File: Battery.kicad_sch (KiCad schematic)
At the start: 4 parts

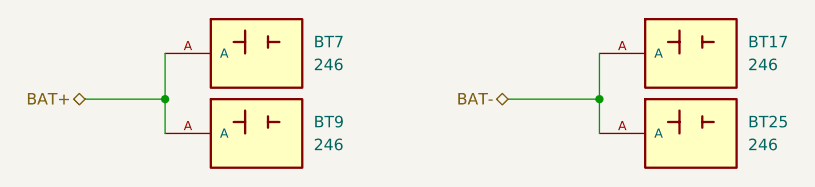
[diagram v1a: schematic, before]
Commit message: adds connectors and bom
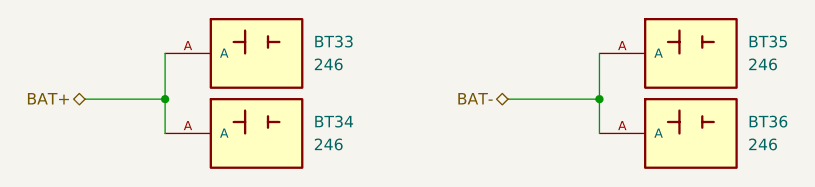
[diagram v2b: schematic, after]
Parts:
- renumbered BT7 to BT33, BT9 to BT34, BT17 to BT35, BT25 to BT36
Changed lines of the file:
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@@
 		(dnp no)
 		(fields_autoplaced yes)
-		(property "Reference" "BT17"
+		(property "Reference" "BT35"
 			(at 125.73 80.0099 0)
 			(effects
@@
 		(instances
 			(project "BounceBack"
-				(path "/f4d3aea2-c6b7-478e-bd31-9b0098518f48/1a31741d-88c3-47d9-834f-01dfee5cc6d9/1551cce4-8866-4495-982a-a77f6e9327d9"
-					(reference "BT17")
-					(unit 1)
-				)
-				(path "/f4d3aea2-c6b7-478e-bd31-9b0098518f48/1a31741d-88c3-47d9-834f-01dfee5cc6d9/117ef703-b8fc-4370-bfcd-aff31c8bd2d5"
-					(reference "BT18")
-					(unit 1)
-				)
-				(path "/f4d3aea2-c6b7-478e-bd31-9b0098518f48/1a31741d-88c3-47d9-834f-01dfee5cc6d9/b6448387-a56d-4315-8544-a7512868ec52"
-					(reference "BT19")
-					(unit 1)
-				)
-				(path "/f4d3aea2-c6b7-478e-bd31-9b0098518f48/1a31741d-88c3-47d9-834f-01dfee5cc6d9/84fcc5dc-fa9b-4edf-8bba-1647bc64b9b8"
-					(reference "BT20")
-					(unit 1)
-				)
-				(path "/f4d3aea2-c6b7-478e-bd31-9b0098518f48/1a31741d-88c3-47d9-834f-01dfee5cc6d9/918d9447-f370-4db2-b8a3-eec52e987d54"
-					(reference "BT21")
-					(unit 1)
-				)
-				(path "/f4d3aea2-c6b7-478e-bd31-9b0098518f48/1a31741d-88c3-47d9-834f-01dfee5cc6d9/c0fa25f9-89d7-46c1-befa-1ac9188fe79f"
-					(reference "BT22")
-					(unit 1)
-				)
-				(path "/f4d3aea2-c6b7-478e-bd31-9b0098518f48/1a31741d-88c3-47d9-834f-01dfee5cc6d9/1a201732-b9ac-4a68-82dc-a3b4e58f320a"
-					(reference "BT23")
-					(unit 1)
-				)
-				(path "/f4d3aea2-c6b7-478e-bd31-9b0098518f48/1a31741d-88c3-47d9-834f-01dfee5cc6d9/9db08163-0bb8-4c3b-bb41-74c13cb1f83a"
-					(reference "BT24")
+				(path "/f4d3aea2-c6b7-478e-bd31-9b0098518f48/afea23a1-6496-4589-887c-166f848f4c04"
+					(reference "BT35")
+					(unit 1)
+				)
+				(path "/f4d3aea2-c6b7-478e-bd31-9b0098518f48/0f47bd77-c5ca-4c02-ab98-3a520c3cd326"
+					(reference "BT39")
 					(unit 1)
 				)
@@
 		(dnp no)
 		(fields_autoplaced yes)
-		(property "Reference" "BT7"
+		(property "Reference" "BT33"
 			(at 77.47 80.0099 0)
 			(effects
@@
 		(instances
 			(project "BounceBack"
-				(path "/f4d3aea2-c6b7-478e-bd31-9b0098518f48/1a31741d-88c3-47d9-834f-01dfee5cc6d9/1a201732-b9ac-4a68-82dc-a3b4e58f320a"
-					(reference "BT7")
-					(unit 1)
-				)
-				(path "/f4d3aea2-c6b7-478e-bd31-9b0098518f48/1a31741d-88c3-47d9-834f-01dfee5cc6d9/1551cce4-8866-4495-982a-a77f6e9327d9"
-					(reference "BT1")
-					(unit 1)
-				)
-				(path "/f4d3aea2-c6b7-478e-bd31-9b0098518f48/1a31741d-88c3-47d9-834f-01dfee5cc6d9/117ef703-b8fc-4370-bfcd-aff31c8bd2d5"
-					(reference "BT2")
-					(unit 1)
-				)
-				(path "/f4d3aea2-c6b7-478e-bd31-9b0098518f48/1a31741d-88c3-47d9-834f-01dfee5cc6d9/b6448387-a56d-4315-8544-a7512868ec52"
-					(reference "BT3")
-					(unit 1)
-				)
-				(path "/f4d3aea2-c6b7-478e-bd31-9b0098518f48/1a31741d-88c3-47d9-834f-01dfee5cc6d9/84fcc5dc-fa9b-4edf-8bba-1647bc64b9b8"
-					(reference "BT4")
-					(unit 1)
-				)
-				(path "/f4d3aea2-c6b7-478e-bd31-9b0098518f48/1a31741d-88c3-47d9-834f-01dfee5cc6d9/918d9447-f370-4db2-b8a3-eec52e987d54"
-					(reference "BT5")
-					(unit 1)
-				)
-				(path "/f4d3aea2-c6b7-478e-bd31-9b0098518f48/1a31741d-88c3-47d9-834f-01dfee5cc6d9/c0fa25f9-89d7-46c1-befa-1ac9188fe79f"
-					(reference "BT6")
-					(unit 1)
-				)
-				(path "/f4d3aea2-c6b7-478e-bd31-9b0098518f48/1a31741d-88c3-47d9-834f-01dfee5cc6d9/9db08163-0bb8-4c3b-bb41-74c13cb1f83a"
-					(reference "BT8")
+				(path "/f4d3aea2-c6b7-478e-bd31-9b0098518f48/afea23a1-6496-4589-887c-166f848f4c04"
+					(reference "BT33")
+					(unit 1)
+				)
+				(path "/f4d3aea2-c6b7-478e-bd31-9b0098518f48/0f47bd77-c5ca-4c02-ab98-3a520c3cd326"
+					(reference "BT37")
 					(unit 1)
 				)
@@
 		(dnp no)
 		(fields_autoplaced yes)
-		(property "Reference" "BT9"
+		(property "Reference" "BT34"
 			(at 77.47 88.8999 0)
 			(effects
@@
 		(instances
 			(project "BounceBack"
-				(path "/f4d3aea2-c6b7-478e-bd31-9b0098518f48/1a31741d-88c3-47d9-834f-01dfee5cc6d9/1551cce4-8866-4495-982a-a77f6e9327d9"
-					(reference "BT9")
-					(unit 1)
-				)
-				(path "/f4d3aea2-c6b7-478e-bd31-9b0098518f48/1a31741d-88c3-47d9-834f-01dfee5cc6d9/117ef703-b8fc-4370-bfcd-aff31c8bd2d5"
-					(reference "BT10")
-					(unit 1)
-				)
-				(path "/f4d3aea2-c6b7-478e-bd31-9b0098518f48/1a31741d-88c3-47d9-834f-01dfee5cc6d9/b6448387-a56d-4315-8544-a7512868ec52"
-					(reference "BT11")
-					(unit 1)
-				)
-				(path "/f4d3aea2-c6b7-478e-bd31-9b0098518f48/1a31741d-88c3-47d9-834f-01dfee5cc6d9/84fcc5dc-fa9b-4edf-8bba-1647bc64b9b8"
-					(reference "BT12")
-					(unit 1)
-				)
-				(path "/f4d3aea2-c6b7-478e-bd31-9b0098518f48/1a31741d-88c3-47d9-834f-01dfee5cc6d9/918d9447-f370-4db2-b8a3-eec52e987d54"
-					(reference "BT13")
-					(unit 1)
-				)
-				(path "/f4d3aea2-c6b7-478e-bd31-9b0098518f48/1a31741d-88c3-47d9-834f-01dfee5cc6d9/c0fa25f9-89d7-46c1-befa-1ac9188fe79f"
-					(reference "BT14")
-					(unit 1)
-				)
-				(path "/f4d3aea2-c6b7-478e-bd31-9b0098518f48/1a31741d-88c3-47d9-834f-01dfee5cc6d9/1a201732-b9ac-4a68-82dc-a3b4e58f320a"
-					(reference "BT15")
-					(unit 1)
-				)
-				(path "/f4d3aea2-c6b7-478e-bd31-9b0098518f48/1a31741d-88c3-47d9-834f-01dfee5cc6d9/9db08163-0bb8-4c3b-bb41-74c13cb1f83a"
-					(reference "BT16")
+				(path "/f4d3aea2-c6b7-478e-bd31-9b0098518f48/afea23a1-6496-4589-887c-166f848f4c04"
+					(reference "BT34")
+					(unit 1)
+				)
+				(path "/f4d3aea2-c6b7-478e-bd31-9b0098518f48/0f47bd77-c5ca-4c02-ab98-3a520c3cd326"
+					(reference "BT38")
 					(unit 1)
 				)
@@
 		(dnp no)
 		(fields_autoplaced yes)
-		(property "Reference" "BT25"
+		(property "Reference" "BT36"
 			(at 125.73 88.8999 0)
 			(effects
@@
 		(instances
 			(project "BounceBack"
-				(path "/f4d3aea2-c6b7-478e-bd31-9b0098518f48/1a31741d-88c3-47d9-834f-01dfee5cc6d9/1551cce4-8866-4495-982a-a77f6e9327d9"
-					(reference "BT25")
-					(unit 1)
-				)
-				(path "/f4d3aea2-c6b7-478e-bd31-9b0098518f48/1a31741d-88c3-47d9-834f-01dfee5cc6d9/117ef703-b8fc-4370-bfcd-aff31c8bd2d5"
-					(reference "BT26")
-					(unit 1)
-				)
-				(path "/f4d3aea2-c6b7-478e-bd31-9b0098518f48/1a31741d-88c3-47d9-834f-01dfee5cc6d9/b6448387-a56d-4315-8544-a7512868ec52"
-					(reference "BT27")
-					(unit 1)
-				)
-				(path "/f4d3aea2-c6b7-478e-bd31-9b0098518f48/1a31741d-88c3-47d9-834f-01dfee5cc6d9/84fcc5dc-fa9b-4edf-8bba-1647bc64b9b8"
-					(reference "BT28")
-					(unit 1)
-				)
-				(path "/f4d3aea2-c6b7-478e-bd31-9b0098518f48/1a31741d-88c3-47d9-834f-01dfee5cc6d9/918d9447-f370-4db2-b8a3-eec52e987d54"
-					(reference "BT29")
-					(unit 1)
-				)
-				(path "/f4d3aea2-c6b7-478e-bd31-9b0098518f48/1a31741d-88c3-47d9-834f-01dfee5cc6d9/c0fa25f9-89d7-46c1-befa-1ac9188fe79f"
-					(reference "BT30")
-					(unit 1)
-				)
-				(path "/f4d3aea2-c6b7-478e-bd31-9b0098518f48/1a31741d-88c3-47d9-834f-01dfee5cc6d9/1a201732-b9ac-4a68-82dc-a3b4e58f320a"
-					(reference "BT31")
-					(unit 1)
-				)
-				(path "/f4d3aea2-c6b7-478e-bd31-9b0098518f48/1a31741d-88c3-47d9-834f-01dfee5cc6d9/9db08163-0bb8-4c3b-bb41-74c13cb1f83a"
-					(reference "BT32")
-					(unit 1)
-				)
+				(path "/f4d3aea2-c6b7-478e-bd31-9b0098518f48/afea23a1-6496-4589-887c-166f848f4c04"
+					(reference "BT36")
+					(unit 1)
+				)
+				(path "/f4d3aea2-c6b7-478e-bd31-9b0098518f48/0f47bd77-c5ca-4c02-ab98-3a520c3cd326"
+					(reference "BT40")
+					(unit 1)
+				)
